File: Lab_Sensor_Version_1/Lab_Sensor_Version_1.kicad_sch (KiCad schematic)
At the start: 28 parts, among them U1 ESP32-POE, U2 AM2302, U3 SSD1306, U4 INMP441

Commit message: Updated Cad Models & Board Layout
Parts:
- added H1, H2, H3: MountingHole, MountingHole:MountingHole_2.2mm_M2, symbol Mechanical:MountingHole
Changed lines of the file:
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@@
+	)
+	(symbol
+		(lib_id "Mechanical:MountingHole")
+		(at 58.42 184.15 0)
+		(unit 1)
+		(exclude_from_sim no)
+		(in_bom no)
+		(on_board yes)
+		(dnp no)
+		(fields_autoplaced yes)
+		(property "Reference" "H3"
+			(at 60.96 182.8799 0)
+			(effects
+				(font
+					(size 1.27 1.27)
+				)
+				(justify left)
+			)
+		)
+		(property "Value" "MountingHole"
+			(at 60.96 185.4199 0)
+			(effects
+				(font
+					(size 1.27 1.27)
+				)
+				(justify left)
+			)
+		)
+		(property "Footprint" "MountingHole:MountingHole_2.2mm_M2"
+			(at 58.42 184.15 0)
+			(effects
+				(font
+					(size 1.27 1.27)
+				)
+				(hide yes)
+			)
+		)
+		(property "Datasheet" "~"
+			(at 58.42 184.15 0)
+			(effects
+				(font
+					(size 1.27 1.27)
+				)
+				(hide yes)
+			)
+		)
+		(property "Description" "Mounting Hole without connection"
+			(at 58.42 184.15 0)
+			(effects
+				(font
+					(size 1.27 1.27)
+				)
+				(hide yes)
+			)
+		)
+		(instances
+			(project ""
+				(path "/37cc0d69-8e3e-4377-b528-04310444116a"
+					(reference "H3")
+					(unit 1)
+				)
+			)
+		)
 	)
 	(symbol
@@
 	)
 	(symbol
+		(lib_id "Mechanical:MountingHole")
+		(at 80.01 184.15 0)
+		(unit 1)
+		(exclude_from_sim no)
+		(in_bom no)
+		(on_board yes)
+		(dnp no)
+		(fields_autoplaced yes)
+		(property "Reference" "H2"
+			(at 82.55 182.8799 0)
+			(effects
+				(font
+					(size 1.27 1.27)
+				)
+				(justify left)
+			)
+		)
+		(property "Value" "MountingHole"
+			(at 82.55 185.4199 0)
+			(effects
+				(font
+					(size 1.27 1.27)
+				)
+				(justify left)
+			)
+		)
+		(property "Footprint" "MountingHole:MountingHole_2.2mm_M2"
+			(at 80.01 184.15 0)
+			(effects
+				(font
+					(size 1.27 1.27)
+				)
+				(hide yes)
+			)
+		)
+		(property "Datasheet" "~"
+			(at 80.01 184.15 0)
+			(effects
+				(font
+					(size 1.27 1.27)
+				)
+				(hide yes)
+			)
+		)
+		(property "Description" "Mounting Hole without connection"
+			(at 80.01 184.15 0)
+			(effects
+				(font
+					(size 1.27 1.27)
+				)
+				(hide yes)
+			)
+		)
+		(instances
+			(project ""
+				(path "/37cc0d69-8e3e-4377-b528-04310444116a"
+					(reference "H2")
+					(unit 1)
+				)
+			)
+		)
+	)
+	(symbol
 		(lib_id "Device:R_Small_US")
 		(at 151.13 72.39 0)
@@
 					(unit 1)
 				)
+			)
+		)
+	)
+	(symbol
+		(lib_id "Mechanical:MountingHole")
+		(at 55.88 167.64 0)
+		(unit 1)
+		(exclude_from_sim no)
+		(in_bom no)
+		(on_board yes)
+		(dnp no)
+		(fields_autoplaced yes)
+		(property "Reference" "H1"
+			(at 58.42 166.3699 0)
+			(effects
+				(font
+					(size 1.27 1.27)
+				)
+				(justify left)
+			)
+		)
+		(property "Value" "MountingHole"
+			(at 58.42 168.9099 0)
+			(effects
+				(font
+					(size 1.27 1.27)
+				)
+				(justify left)
+			)
+		)
+		(property "Footprint" "MountingHole:MountingHole_2.2mm_M2"
+			(at 55.88 167.64 0)
+			(effects
+				(font
+					(size 1.27 1.27)
+				)
+				(hide yes)
+			)
+		)
+		(property "Datasheet" "~"
+			(at 55.88 167.64 0)
+			(effects
+				(font
+					(size 1.27 1.27)
+				)
+				(hide yes)
+			)
+		)
+		(property "Description" "Mounting Hole without connection"
+			(at 55.88 167.64 0)
+			(effects
+				(font
+					(size 1.27 1.27)
+				)
+				(hide yes)
+			)
+		)
+		(instances
+			(project ""
+				(path "/37cc0d69-8e3e-4377-b528-04310444116a"
+					(reference "H1")
+					(unit 1)
+				)

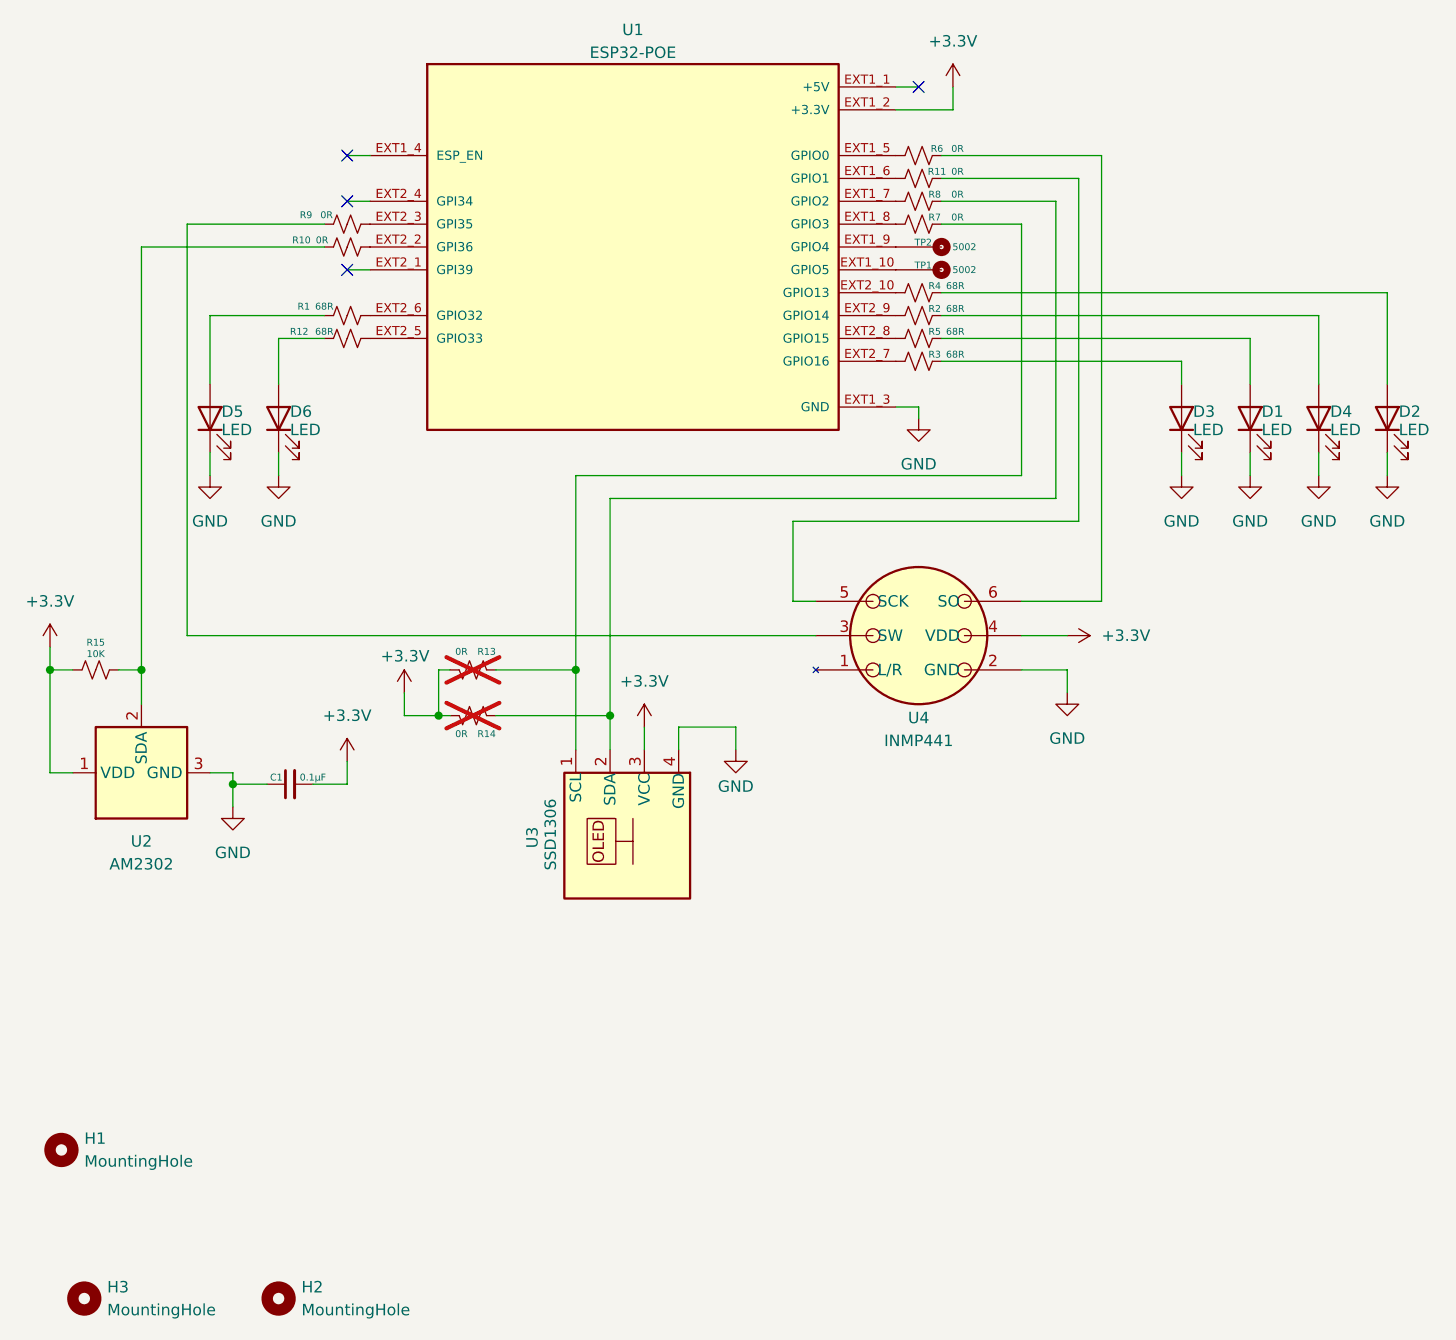
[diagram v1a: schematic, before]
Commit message: Changed pinout to work with Code
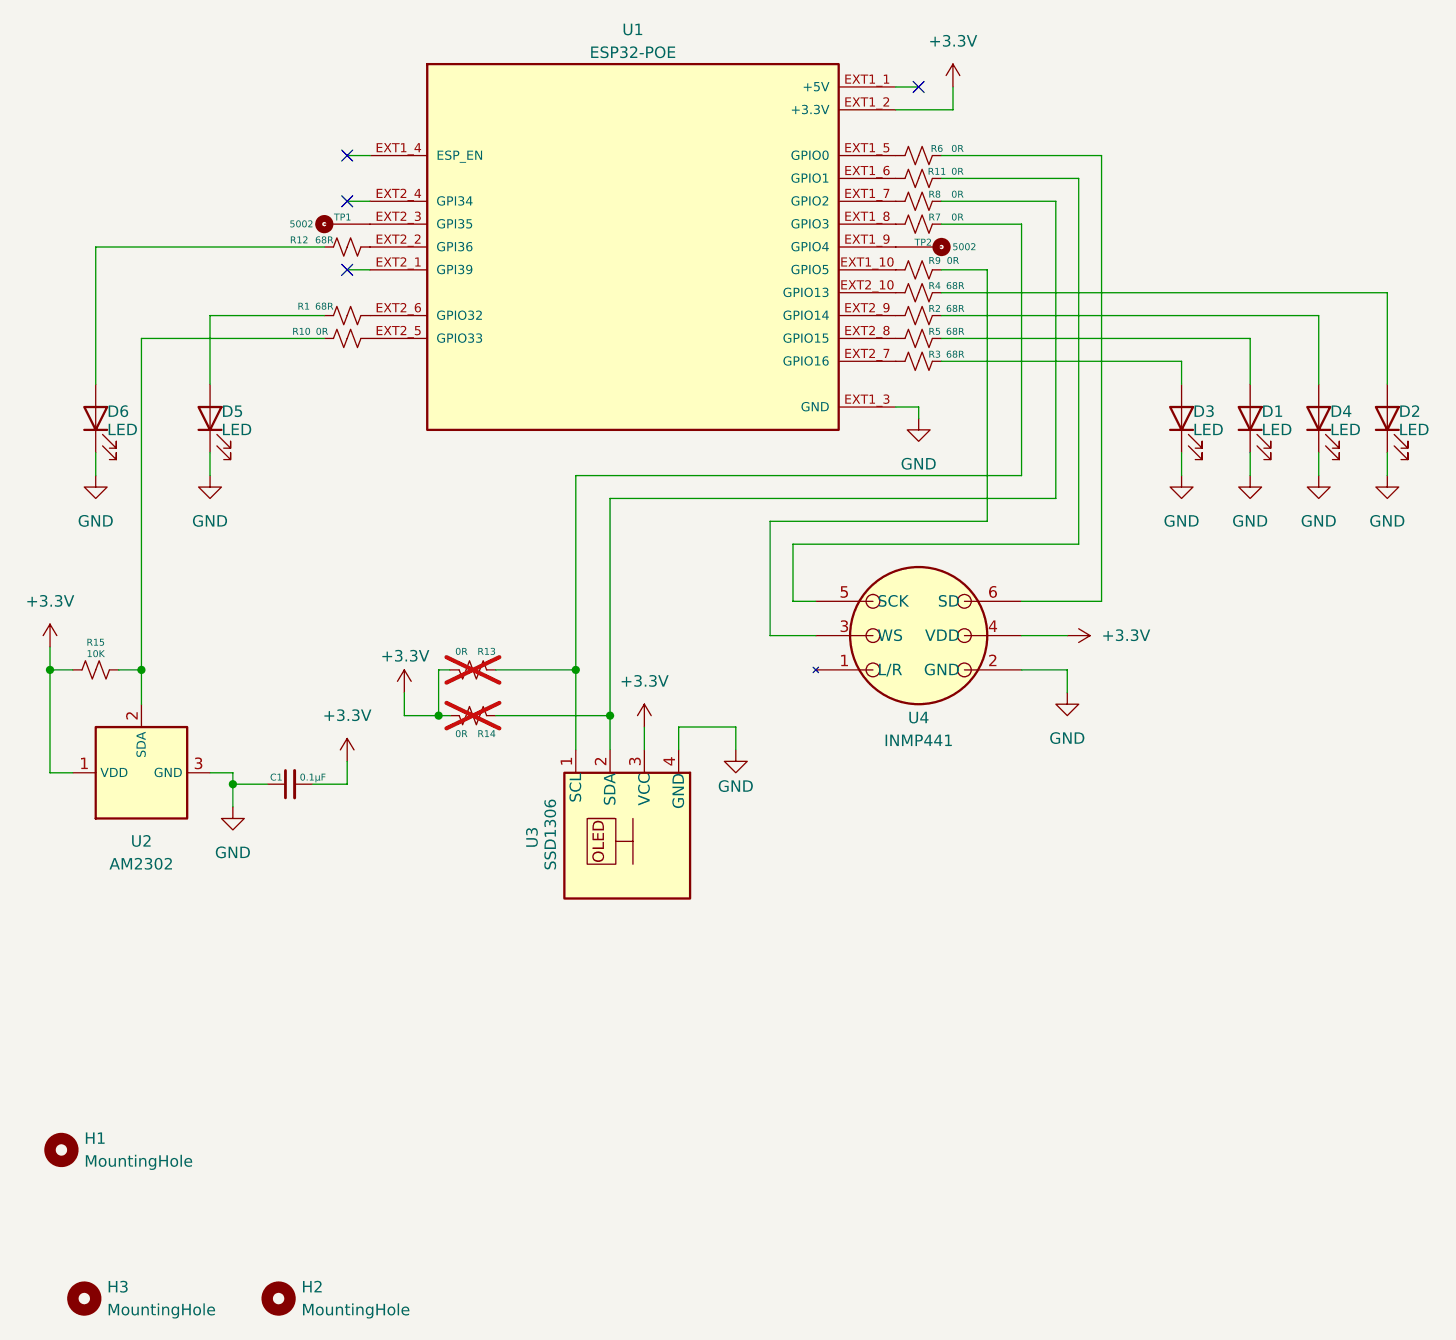
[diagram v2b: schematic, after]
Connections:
- net at R9.1: now also U1.EXT1_10 (GPIO5); no longer U1.EXT2_3 (GPI35)
- net at R10.1: now also U1.EXT2_5 (GPIO33); no longer U1.EXT2_2 (GPI36)
- net at TP1.TP: now also U1.EXT2_3 (GPI35); no longer U1.EXT1_10 (GPIO5)
- net at R12.1: now also U1.EXT2_2 (GPI36); no longer U1.EXT2_5 (GPIO33)
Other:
- moved on the sheet: D6, R10, R12, R9, TP1
